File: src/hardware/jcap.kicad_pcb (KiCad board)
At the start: 2 copper layers, 136.8 x 87 mm, 66 parts, among them J201 CPU PGMR, J202 SPARE CPU HDR, J203 GPU PGMR, J204 SPARE GPU HDR, J301 DC IN, J501 VGA OUT, J601 CONTROLS, Q301 IPP80P03P4L-04, SW201 CPU ~{RES}, SW202 DEBUG, SW203 GPU ~{RES}, SW601 TILT, U201 P8X32A, U202 P8X32A, U301 LM3940IT, U401 24LC256, U402 24LC256, U601 74HC165, U602 74HC165, Y201 6.5MHz, Y202 6.5MHz

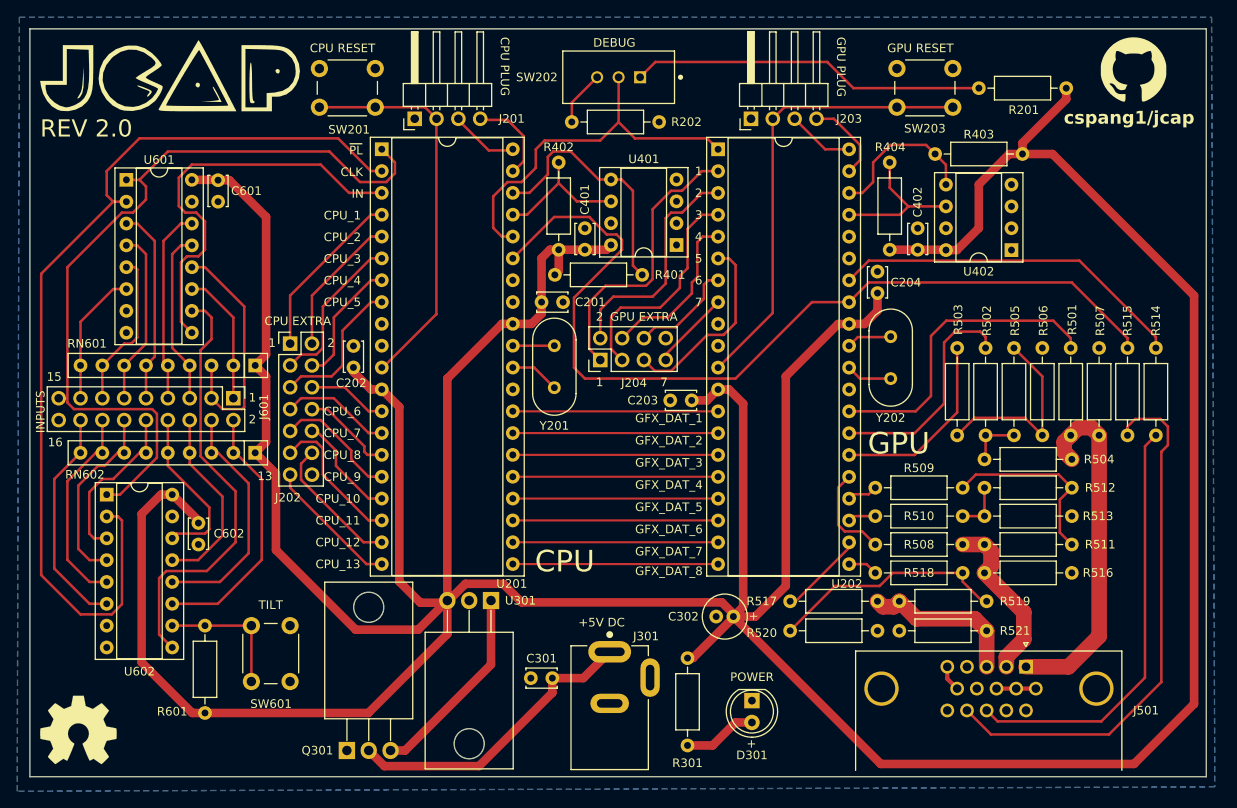
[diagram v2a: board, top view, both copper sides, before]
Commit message: Added second gnd to input hdr
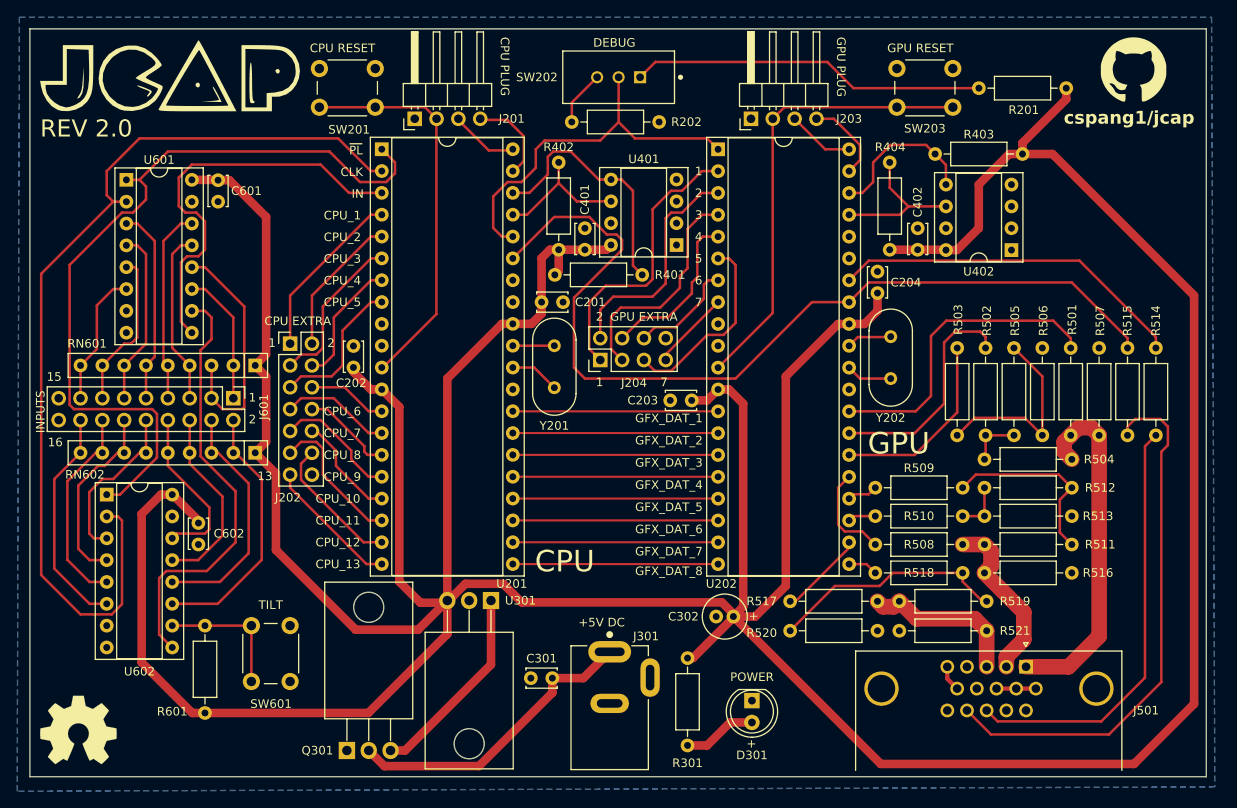
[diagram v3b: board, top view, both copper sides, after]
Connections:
- J601 pad 17: unconnected-(J601-Pin_17-Pad17) -> GND
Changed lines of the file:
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@@
   (net 103 "Net-(R202-Pad1)")
   (net 104 "Net-(Q301-D)")
-  (net 105 "unconnected-(J601-Pin_17-Pad17)")
   (footprint "Package_TO_SOT_THT:TO-220-3_Horizontal_TabDown" (layer "F.Cu")
     (at 114.554 135.341)
@@
       (net 60 "/Input/IN16") (pinfunction "Pin_16") (pintype "passive"))
     (pad "17" thru_hole oval (at 0 20.32 270) (size 1.7 1.7) (drill 1) (layers "*.Cu" "*.Mask")
-      (net 105 "unconnected-(J601-Pin_17-Pad17)") (pinfunction "Pin_17") (pintype "passive+no_connect"))
+      (net 2 "GND") (pinfunction "Pin_17") (pintype "passive"))
     (pad "18" thru_hole oval (at 2.54 20.32 270) (size 1.7 1.7) (drill 1) (layers "*.Cu" "*.Mask")
       (net 2 "GND") (pinfunction "Pin_18") (pintype "passive"))
@@
     (property "ki_keywords" "microcontroller multicore Parallax Propeller DIP")
     (attr through_hole)
-    (fp_text reference "U202" (at 14.986 50.546) (layer "F.SilkS")
+    (fp_text reference "U202" (at 0.381 50.546) (layer "F.SilkS")
         (effects (font (size 1 1) (thickness 0.15)))
     )
@@
   (segment (start 194.701 128.143) (end 190.121 128.143) (width 0.5) (layer "F.Cu") (net 2))
   (segment (start 184.396 126.998) (end 185.541 128.143) (width 0.5) (layer "F.Cu") (net 2))
-  (segment (start 157.0925 134.7535) (end 159.766 132.08) (width 1) (layer "F.Cu") (net 3))
-  (segment (start 159.766 132.08) (end 161.671 132.08) (width 1) (layer "F.Cu") (net 3))
-  (segment (start 154.178 134.7535) (end 157.0925 134.7535) (width 1) (layer "F.Cu") (net 3))
+  (segment (start 159.131 132.08) (end 161.671 132.08) (width 1) (layer "F.Cu") (net 3))
+  (segment (start 154.178 134.7535) (end 156.4575 134.7535) (width 1) (layer "F.Cu") (net 3))
+  (segment (start 156.4575 134.7535) (end 159.131 132.08) (width 1) (layer "F.Cu") (net 3))
   (segment (start 124.968 61.986) (end 124.968 84.572) (width 0.3) (layer "F.Cu") (net 4))
   (segment (start 123.646 60.512) (end 117.856 60.512) (width 0.3) (layer "F.Cu") (net 4))
@@
   (segment (start 140.97 82.677) (end 140.97 90.805) (width 0.3) (layer "F.Cu") (net 44))
   (segment (start 168.656 83.185) (end 172.974 83.185) (width 0.3) (layer "F.Cu") (net 44))
+  (segment (start 83.566 90.551) (end 85.471 88.646) (width 0.3) (layer "F.Cu") (net 45))
+  (segment (start 85.471 83.566) (end 87.376 81.661) (width 0.3) (layer "F.Cu") (net 45))
   (segment (start 87.376 81.661) (end 88.9 81.661) (width 0.3) (layer "F.Cu") (net 45))
-  (segment (start 83.566 90.551) (end 83.566 85.471) (width 0.3) (layer "F.Cu") (net 45))
-  (segment (start 83.566 85.471) (end 87.376 81.661) (width 0.3) (layer "F.Cu") (net 45))
+  (segment (start 85.471 88.646) (end 85.471 83.566) (width 0.3) (layer "F.Cu") (net 45))
   (segment (start 83.566 94.366) (end 83.566 90.551) (width 0.3) (layer "F.Cu") (net 45))
   (segment (start 86.106 94.366) (end 86.106 90.551) (width 0.3) (layer "F.Cu") (net 46))
@@
   (segment (start 144.018 64.389) (end 137.541 64.389) (width 0.3) (layer "F.Cu") (net 61))
   (segment (start 133.246654 69.215) (end 131.572 70.889654) (width 0.3) (layer "F.Cu") (net 61))
+  (segment (start 82.296 78.867) (end 82.296 95.123) (width 0.3) (layer "F.Cu") (net 62))
   (segment (start 116.078 69.215) (end 119.126 69.215) (width 0.3) (layer "F.Cu") (net 62))
-  (segment (start 82.804 95.631) (end 91.905028 95.631) (width 0.3) (layer "F.Cu") (net 62))
-  (segment (start 92.456 101.270173) (end 88.149173 105.577) (width 0.3) (layer "F.Cu") (net 62))
+  (segment (start 82.296 95.123) (end 82.804 95.631) (width 0.3) (layer "F.Cu") (net 62))
   (segment (start 119.126 69.215) (end 120.142 68.199) (width 0.3) (layer "F.Cu") (net 62))
-  (segment (start 91.905028 95.631) (end 92.456 96.181972) (width 0.3) (layer "F.Cu") (net 62))
   (segment (start 88.9 68.961) (end 90.424 68.961) (width 0.3) (layer "F.Cu") (net 62))
   (segment (start 90.424 68.961) (end 93.726 65.659) (width 0.3) (layer "F.Cu") (net 62))
-  (segment (start 89.662 72.771) (end 88.392 72.771) (width 0.3) (layer "F.Cu") (net 62))
-  (segment (start 92.456 96.181972) (end 92.456 101.270173) (width 0.3) (layer "F.Cu") (net 62))
-  (segment (start 88.392 72.771) (end 82.042 79.121) (width 0.3) (layer "F.Cu") (net 62))
+  (segment (start 91.186 69.723) (end 91.186 71.247) (width 0.3) (layer "F.Cu") (net 62))
+  (segment (start 88.149173 105.577) (end 86.614 105.577) (width 0.3) (layer "F.Cu") (net 62))
+  (segment (start 92.456 101.270173) (end 88.149173 105.577) (width 0.3) (layer "F.Cu") (net 62))
   (segment (start 112.522 65.659) (end 116.078 69.215) (width 0.3) (layer "F.Cu") (net 62))
   (segment (start 93.726 65.659) (end 112.522 65.659) (width 0.3) (layer "F.Cu") (net 62))
-  (segment (start 90.424 68.961) (end 91.186 69.723) (width 0.3) (layer "F.Cu") (net 62))
-  (segment (start 88.149173 105.577) (end 86.614 105.577) (width 0.3) (layer "F.Cu") (net 62))
+  (segment (start 91.186 71.247) (end 89.662 72.771) (width 0.3) (layer "F.Cu") (net 62))
+  (segment (start 91.905028 95.631) (end 92.456 96.181972) (width 0.3) (layer "F.Cu") (net 62))
   (segment (start 120.142 66.924) (end 118.613 65.395) (width 0.3) (layer "F.Cu") (net 62))
+  (segment (start 82.804 95.631) (end 91.905028 95.631) (width 0.3) (layer "F.Cu") (net 62))
+  (segment (start 90.424 68.961) (end 91.186 69.723) (width 0.3) (layer "F.Cu") (net 62))
   (segment (start 120.142 68.199) (end 120.142 66.924) (width 0.3) (layer "F.Cu") (net 62))
-  (segment (start 91.186 69.723) (end 91.186 71.247) (width 0.3) (layer "F.Cu") (net 62))
-  (segment (start 82.042 94.869) (end 82.804 95.631) (width 0.3) (layer "F.Cu") (net 62))
-  (segment (start 82.042 79.121) (end 82.042 94.869) (width 0.3) (layer "F.Cu") (net 62))
-  (segment (start 91.186 71.247) (end 89.662 72.771) (width 0.3) (layer "F.Cu") (net 62))
+  (segment (start 92.456 96.181972) (end 92.456 101.270173) (width 0.3) (layer "F.Cu") (net 62))
+  (segment (start 89.662 72.771) (end 88.392 72.771) (width 0.3) (layer "F.Cu") (net 62))
+  (segment (start 88.392 72.771) (end 82.296 78.867) (width 0.3) (layer "F.Cu") (net 62))
   (segment (start 87.376 71.501) (end 78.994 79.883) (width 0.3) (layer "F.Cu") (net 63))
   (segment (start 90.424 64.135) (end 113.538 64.135) (width 0.3) (layer "F.Cu") (net 63))

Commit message: Added GND pins to spare headers
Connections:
- J202 pad 14: unconnected-(J202-Pin_14-Pad14) -> GND
- J204 pad 8: unconnected-(J204-Pin_8-Pad8) -> GND
